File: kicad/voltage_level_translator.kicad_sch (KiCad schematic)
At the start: 16 parts, among them Q1 2N7002, Q2 2N7002, Q3 2N7002, U3 FXMA108, U4 LSF0108PW, U5 LSF0108PW, U6 LSF0108PW

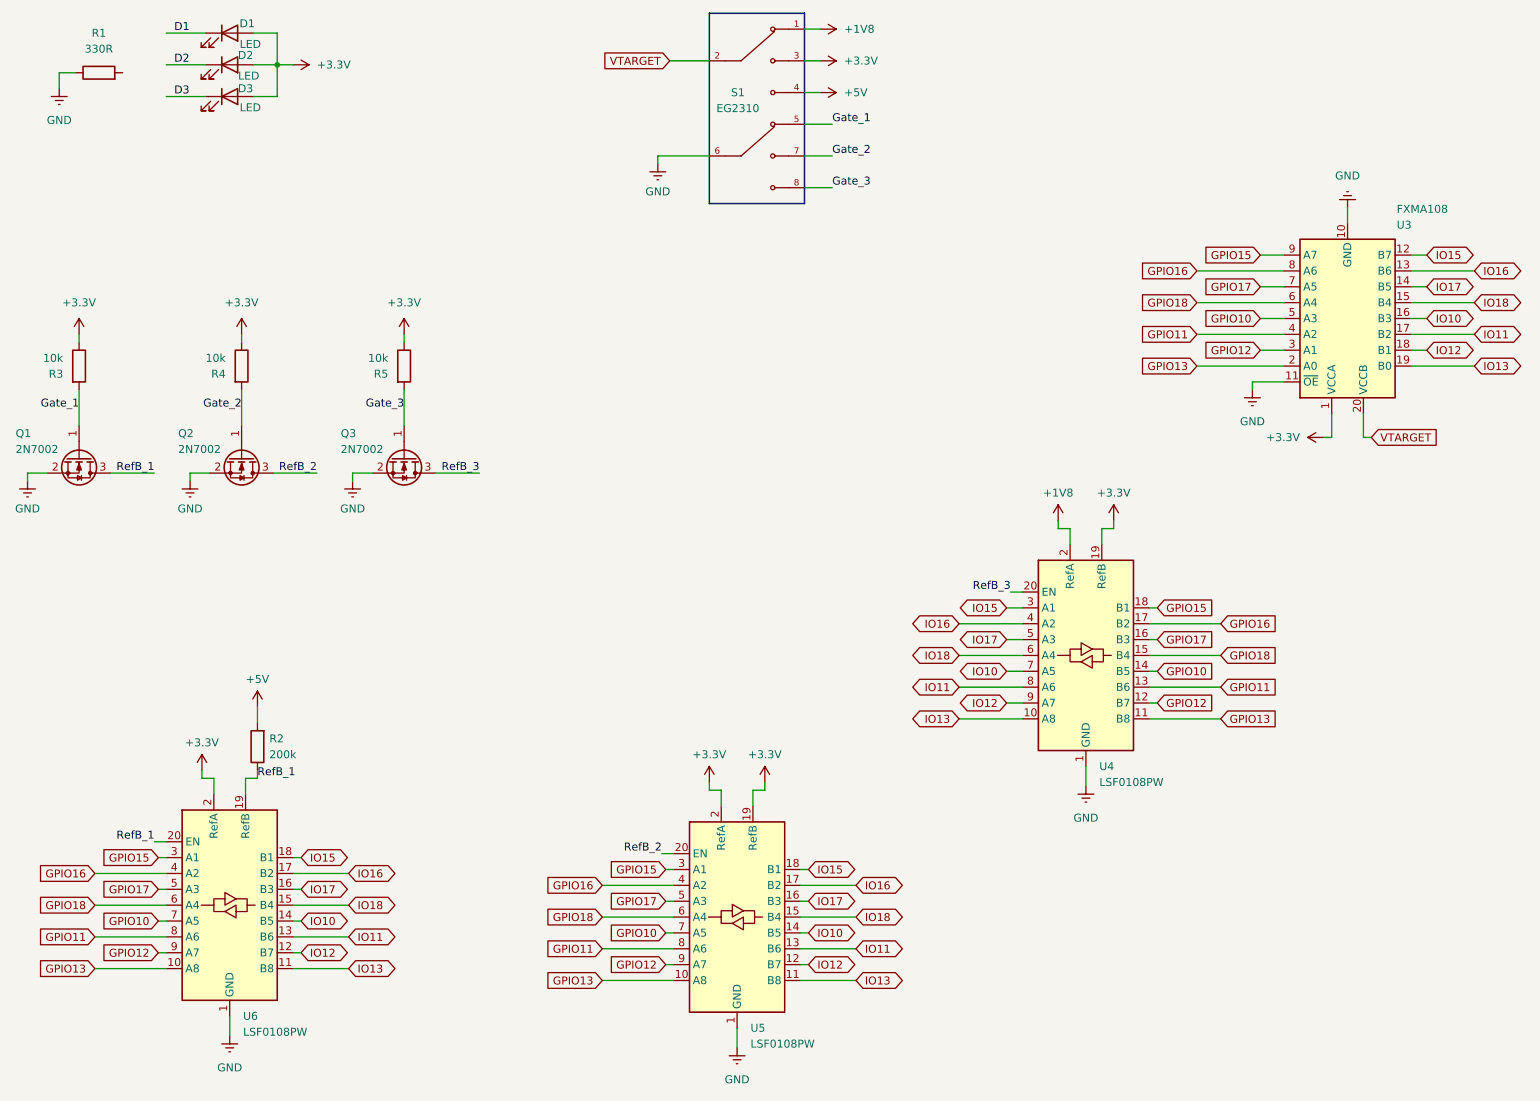
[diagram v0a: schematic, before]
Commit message: Eliminated FXMA108
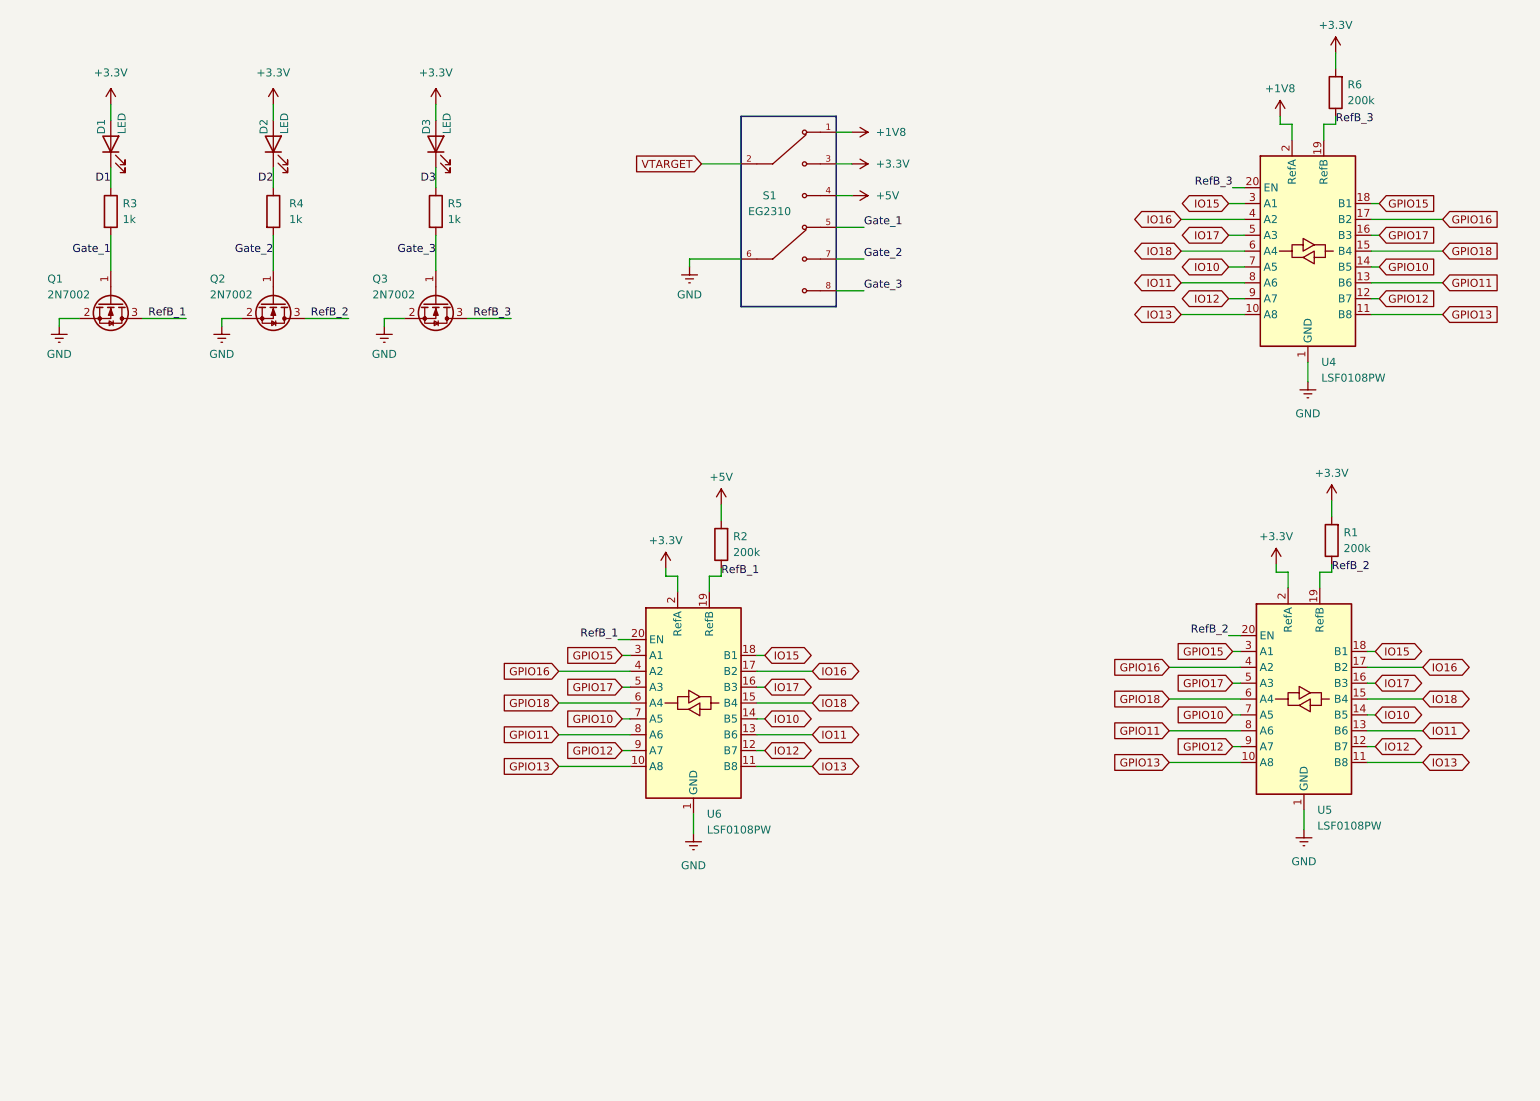
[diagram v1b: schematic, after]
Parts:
- removed U3: FXMA108, Package_DFN_QFN:WQFN-20-1EP_2.5x4.5mm_P0.5mm_EP1x2.9mm, symbol Logic_LevelTranslator:FXMA108
- added R6: 200k, Resistor_SMD:R_0805_2012Metric, symbol Device:R
- R1: value 330R -> 200k
- R3, R4, R5: value 10k -> 1k
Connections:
- net +3.3V: now also R1.2, R6.2; no longer R3.1, R4.1, R5.1, U4.19 (RefB), U5.19 (RefB)
- net D1: now also R3.1
- net D2: now also R4.1
- net D3: now also R5.1
- net GND: no longer R1.1
- net RefB_2: now also R1.1, U5.19 (RefB)
- net RefB_3: now also U4.19 (RefB), R6.1
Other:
- moved on the sheet: D1, Q1, Q2, Q3, R2, R3, R4, R5, S1, U4, U5, U6

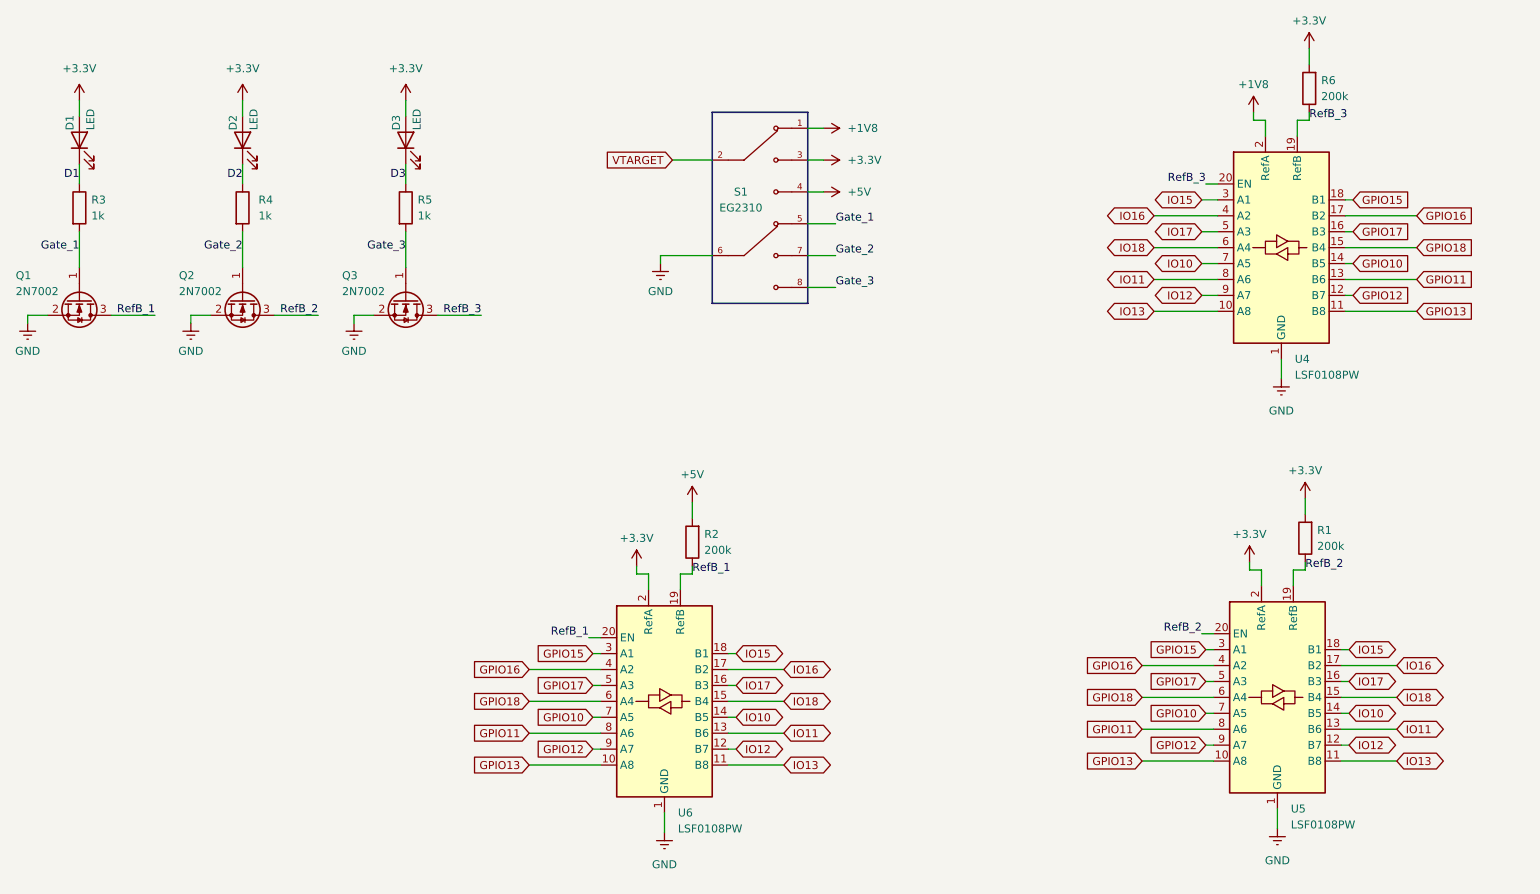
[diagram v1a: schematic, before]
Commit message: Added LSF1080 PCB placeholders
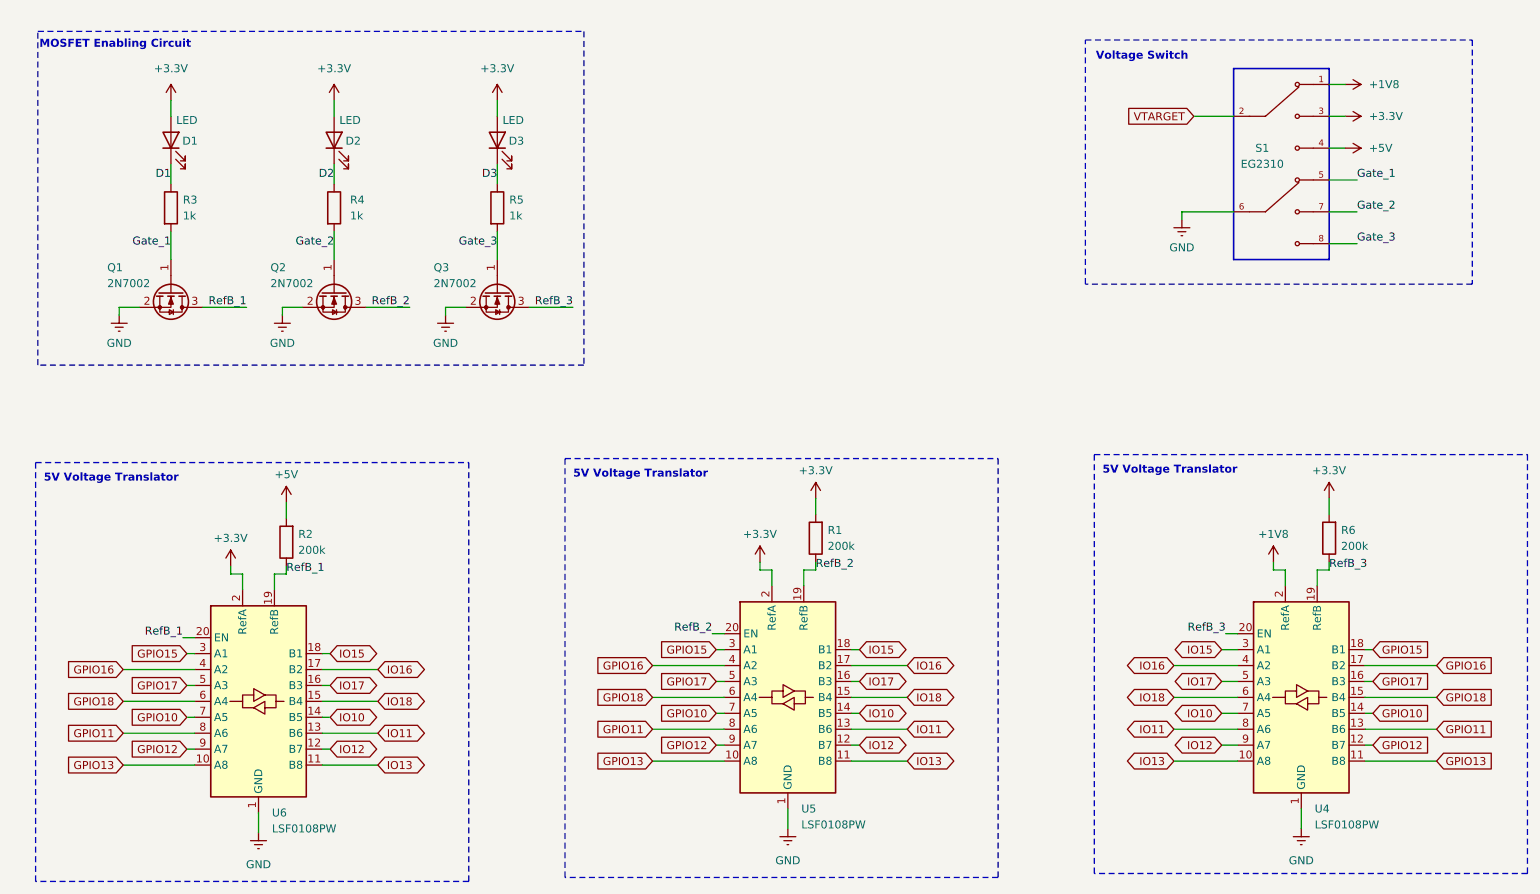
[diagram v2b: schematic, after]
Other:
- note added: "5V Voltage Translator"
- note added: "MOSFET Enabling Circuit"
- note added: "Voltage Switch"
- moved on the sheet: D1, D2, D3, Q1, Q2, Q3, R1, R2, R3, R4, R5, R6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

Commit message: Experimented with wiring
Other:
- note added: "1.8V Voltage Translator"
- note added: "3.3V Voltage Translator"
- moved on the sheet: D1, D2, D3, Q1, Q2, Q3, R1, R2, R3, R4, R5, R6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

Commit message: Updated PCB
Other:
- moved on the sheet: D1, D2, D3, Q1, Q2, Q3, R1, R2, R3, R4, R5, R6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

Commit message: Update voltage_level_translator.kicad_sch
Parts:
- added U3, U7: TMUX1574PW, Package_SO:TSSOP-16_4.4x5mm_P0.65mm, symbol Analog_Switch:TMUX1574PW
- added U8, U9: TXS0108EPW, Package_SO:Texas_PW0020A_TSSOP-20_4.4x6.5mm_P0.65mm, symbol Logic_LevelTranslator:TXS0108EPW
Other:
- moved on the sheet: D1, D2, D3, Q1, Q2, Q3, R1, R2, R3, R4, R5, R6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

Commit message: Update voltage_level_translator.kicad_sch
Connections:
- net +1V8: now also U9.2 (VCCA)
- net +3.3V: now also U8.2 (VCCA), U9.19 (VCCB)
- net GND: now also U3.8 (GND), U7.8 (GND), U8.11 (GND), U9.11 (GND)
- net GPIO10: now also U8.6 (A5), U9.15 (B5)
- net GPIO11: now also U8.7 (A6), U9.14 (B6)
- net GPIO12: now also U8.8 (A7), U9.13 (B7)
- net GPIO13: now also U8.9 (A8), U9.12 (B8)
- net GPIO15: now also U8.1 (A1), U9.20 (B1)
- net GPIO16: now also U8.3 (A2), U9.18 (B2)
- net GPIO17: now also U8.4 (A3), U9.17 (B3)
- net GPIO18: now also U8.5 (A4), U9.16 (B4)
- net IO10: now also U7.4 (D1)
- net IO11: now also U7.7 (D2)
- net IO12: now also U7.9 (D3)
- net IO13: now also U7.12 (D4)
- net IO15: now also U3.4 (D1)
- net IO16: now also U3.7 (D2)
- net IO17: now also U3.9 (D3)
- net IO18: now also U3.12 (D4)
- net VTARGET: now also U8.19 (VCCB)
- net IO13_H: now reaches U8.12 (B8)
- net IO13_H: now also U7.13 (S4B)
- net IO12_H: now reaches U8.13 (B7)
- net IO12_H: now also U7.10 (S3B)
- net IO11_H: now reaches U8.14 (B6)
- net IO11_H: now also U7.6 (S2B)
- net IO10_H: now reaches U8.15 (B5)
- net IO10_H: now also U7.3 (S1B)
- net IO17_H: now reaches U8.17 (B3)
- net IO17_H: now also U3.10 (S3B)
- net IO16_H: now reaches U8.18 (B2)
- net IO16_H: now also U3.6 (S2B)
- net IO15_H: now reaches U8.20 (B1)
- net IO15_H: now also U3.3 (S1B)
- net IO15_L: now reaches U9.1 (A1)
- net IO15_L: now also U3.2 (S1A)
- net IO16_L: now reaches U9.3 (A2)
- net IO16_L: now also U3.5 (S2A)
- net IO17_L: now reaches U9.4 (A3)
- net IO17_L: now also U3.11 (S3A)
- net IO10_L: now reaches U9.6 (A5)
- net IO10_L: now also U7.2 (S1A)
- net IO11_L: now reaches U9.7 (A6)
- net IO11_L: now also U7.5 (S2A)
- net IO12_L: now reaches U9.8 (A7)
- net IO12_L: now also U7.11 (S3A)
- net IO13_L: now reaches U9.9 (A8)
- net IO13_L: now also U7.14 (S4A)
- net IO18_H: now reaches U3.13 (S4B)
- net IO18_L: now reaches U3.14 (S4A)
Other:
- note added: "5V/3.3V Voltage Translator"
- moved on the sheet: S1, U3, U7, U8, U9

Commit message: Updated SEL Logic
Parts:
- removed R1, R2, R6: 200k, Resistor_SMD:R_0805_2012Metric, symbol Device:R
- removed U4, U5, U6: LSF0108PW, Package_SO:TSSOP-20_4.4x6.5mm_P0.65mm, symbol Logic_LevelTranslator:LSF0108PW
- added C5, C6: 0.1u, Capacitor_SMD:C_0805_2012Metric, symbol Device:C
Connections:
- net +3.3V: now also S1.7, S1.8, U3.16 (VDD), U7.16 (VDD), C5.1, C6.1
- net GND: now also S1.5, U3.15 (~{EN}), U7.15 (~{EN}), C5.2, C6.2; no longer S1.6
- net Gate_1: no longer S1.5
- net Gate_2: no longer S1.7
- net Gate_3: no longer S1.8
- net SEL: now reaches U7.1 (SEL)
- net SEL: now also S1.6, U3.1 (SEL)
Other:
- note added: "Multiplexer D1-D4"
- note removed: "3.3V Voltage Translator"
- note removed: "5V Voltage Translator"
- moved on the sheet: D1, D2, D3, Q1, Q2, Q3, R3, R4, R5, S1, U3, U7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
